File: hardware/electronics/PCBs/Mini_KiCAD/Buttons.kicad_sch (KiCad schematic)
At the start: 5 parts

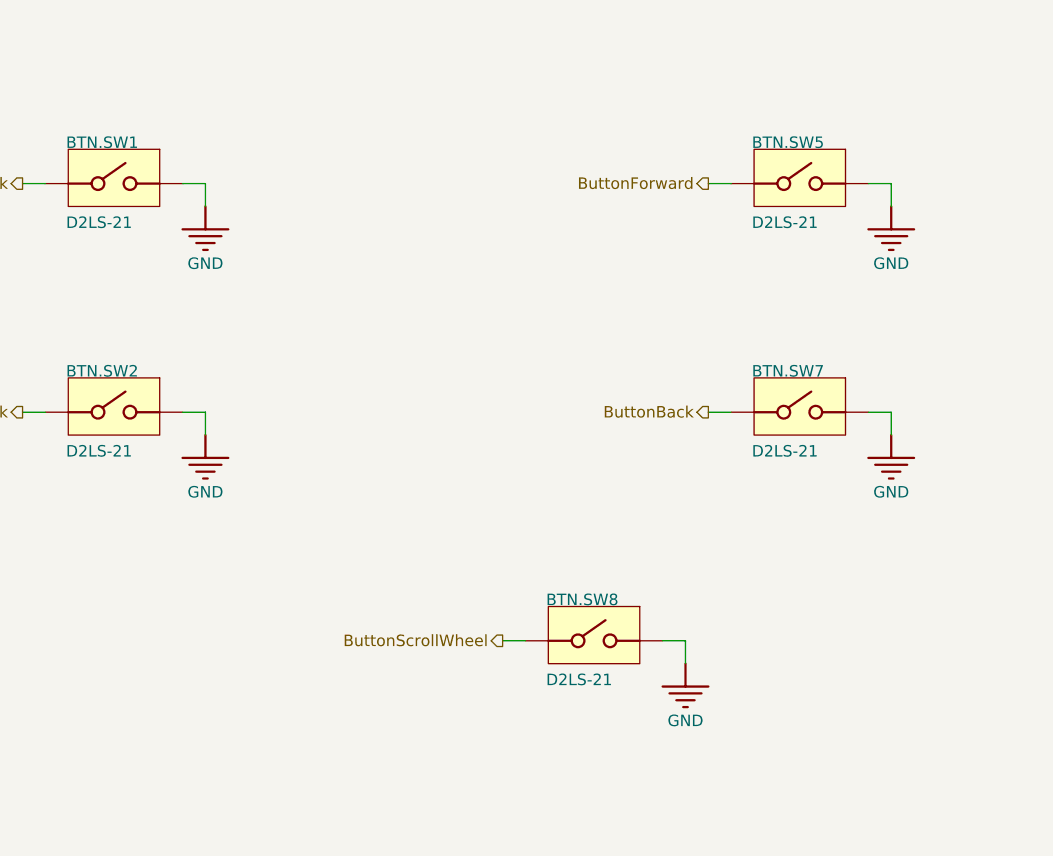
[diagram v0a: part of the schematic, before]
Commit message: Initial commit of the PCB project file replacing the ADNS-5050 with PMW3360, referencing the schematic of the Ploopy Classic.
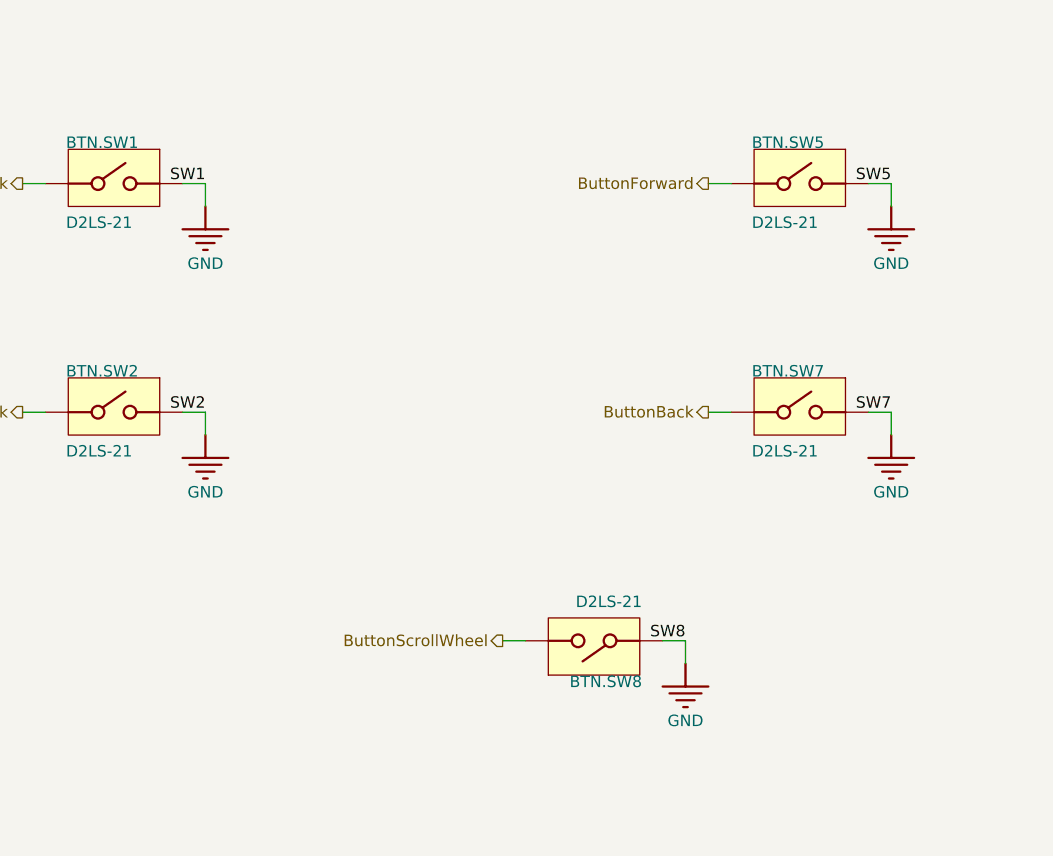
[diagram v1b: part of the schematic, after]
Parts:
- BTN.SW1, BTN.SW2, BTN.SW5, BTN.SW7, BTN.SW8: footprint D2LS-21 -> Switches.PcbLib:D2LS-21
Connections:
- net ButtonScrollWheel: now also BTN.SW8.B; no longer BTN.SW8.A
- net GND: now also BTN.SW8.A; no longer BTN.SW8.B
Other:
- moved on the sheet: BTN.SW8
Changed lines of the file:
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@@
+		)
+	)
+	(label "SW8"
+		(at 177.8 127 180)
+		(fields_autoplaced yes)
+		(effects
+			(font
+				(size 1.27 1.27)
+			)
+			(justify right bottom)
+		)
+	)
+	(label "SW7"
+		(at 200.66 101.6 180)
+		(fields_autoplaced yes)
+		(effects
+			(font
+				(size 1.27 1.27)
+			)
+			(justify right bottom)
+		)
+	)
+	(label "SW2"
+		(at 124.46 101.6 180)
+		(fields_autoplaced yes)
+		(effects
+			(font
+				(size 1.27 1.27)
+			)
+			(justify right bottom)
+		)
+	)
+	(label "SW5"
+		(at 200.66 76.2 180)
+		(fields_autoplaced yes)
+		(effects
+			(font
+				(size 1.27 1.27)
+			)
+			(justify right bottom)
+		)
+	)
+	(label "SW1"
+		(at 124.46 76.2 180)
+		(fields_autoplaced yes)
+		(effects
+			(font
+				(size 1.27 1.27)
+			)
+			(justify right bottom)
 		)
 	)
@@
 	(symbol
 		(lib_id "Mini-altium-import:BTN_0_D2LS-21")
-		(at 167.64 127 0)
+		(at 167.64 127 180)
 		(unit 1)
 		(exclude_from_sim no)
@@
 		(dnp no)
 		(property "Reference" "BTN.SW8"
-			(at 162.306 123.19 0)
+			(at 172.974 130.81 0)
 			(effects
 				(font
@@
 		)
 		(property "Value" "D2LS-21"
-			(at 162.306 132.08 0)
-			(effects
-				(font
-					(size 1.27 1.27)
-				)
-				(justify left bottom)
-			)
-		)
-		(property "Footprint" "D2LS-21"
+			(at 172.974 121.92 0)
+			(effects
+				(font
+					(size 1.27 1.27)
+				)
+				(justify left bottom)
+			)
+		)
+		(property "Footprint" "Switches.PcbLib:D2LS-21"
 			(at 167.64 127 0)
 			(effects
@@
 		)
 		(property "SUPPLIER 1" "Digi-Key"
-			(at 159.512 123.19 0)
+			(at 175.768 130.81 0)
 			(effects
 				(font
@@
 		)
 		(property "SUPPLIER 2" "Mouser"
-			(at 159.512 120.65 0)
+			(at 175.768 133.35 0)
 			(effects
 				(font
@@
 		)
 		(property "SUPPLIER PART NUMBER 1" "Z4378CT-ND"
-			(at 159.512 123.19 0)
+			(at 175.768 130.81 0)
 			(effects
 				(font
@@
 		)
 		(property "SUPPLIER PART NUMBER 2" "653-D2LS-21"
-			(at 159.512 120.65 0)
+			(at 175.768 133.35 0)
 			(effects
 				(font
@@
 			)
 		)
-		(property "Footprint" "D2LS-21"
+		(property "Footprint" "Switches.PcbLib:D2LS-21"
 			(at 190.5 101.6 0)
 			(effects
@@
 			)
 		)
-		(property "Footprint" "D2LS-21"
+		(property "Footprint" "Switches.PcbLib:D2LS-21"
 			(at 114.3 101.6 0)
 			(effects
@@
 			)
 		)
-		(property "Footprint" "D2LS-21"
+		(property "Footprint" "Switches.PcbLib:D2LS-21"
 			(at 114.3 76.2 0)
 			(effects
@@
 			)
 		)
-		(property "Footprint" "D2LS-21"
+		(property "Footprint" "Switches.PcbLib:D2LS-21"
 			(at 190.5 76.2 0)
 			(effects
